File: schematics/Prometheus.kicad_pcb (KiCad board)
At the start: 2 copper layers, 170.2 x 170.2 mm, 57 parts, among them J1 ATX Power Conn, J10 Centronics, J11 ps/2 keyb, J12 Expansion, J13 Joy1, J14 Joy2, J15 rs232, J16 DIN41612_02x32_AB, J17 DIN41612_02x32_AB, J2 FDC Connector, J3 IDE Connector, J4 JTAG, J5 Left Audio, J6 Right Audio, J7 GRACE board interface 1, J8 GRACE board interface 2, J9 15kHz Video Out, SW1 Power Switch, SW2 Reset Switch, U1 DS1501YN, U10 2764, U11 EN5503DOC, U12 VRAM, U13 wdc65c22, U14 wdc65c51, U15 MAX233CPP, U16 wdc65c22, U17 41464, U18 41464, U19 41464, U2 wdc65c816, U20 41464, U3 WD1772, U8 XC9572XL-TQ100, X1 32kHz, X2 8MHz, X3 1.8432MHz

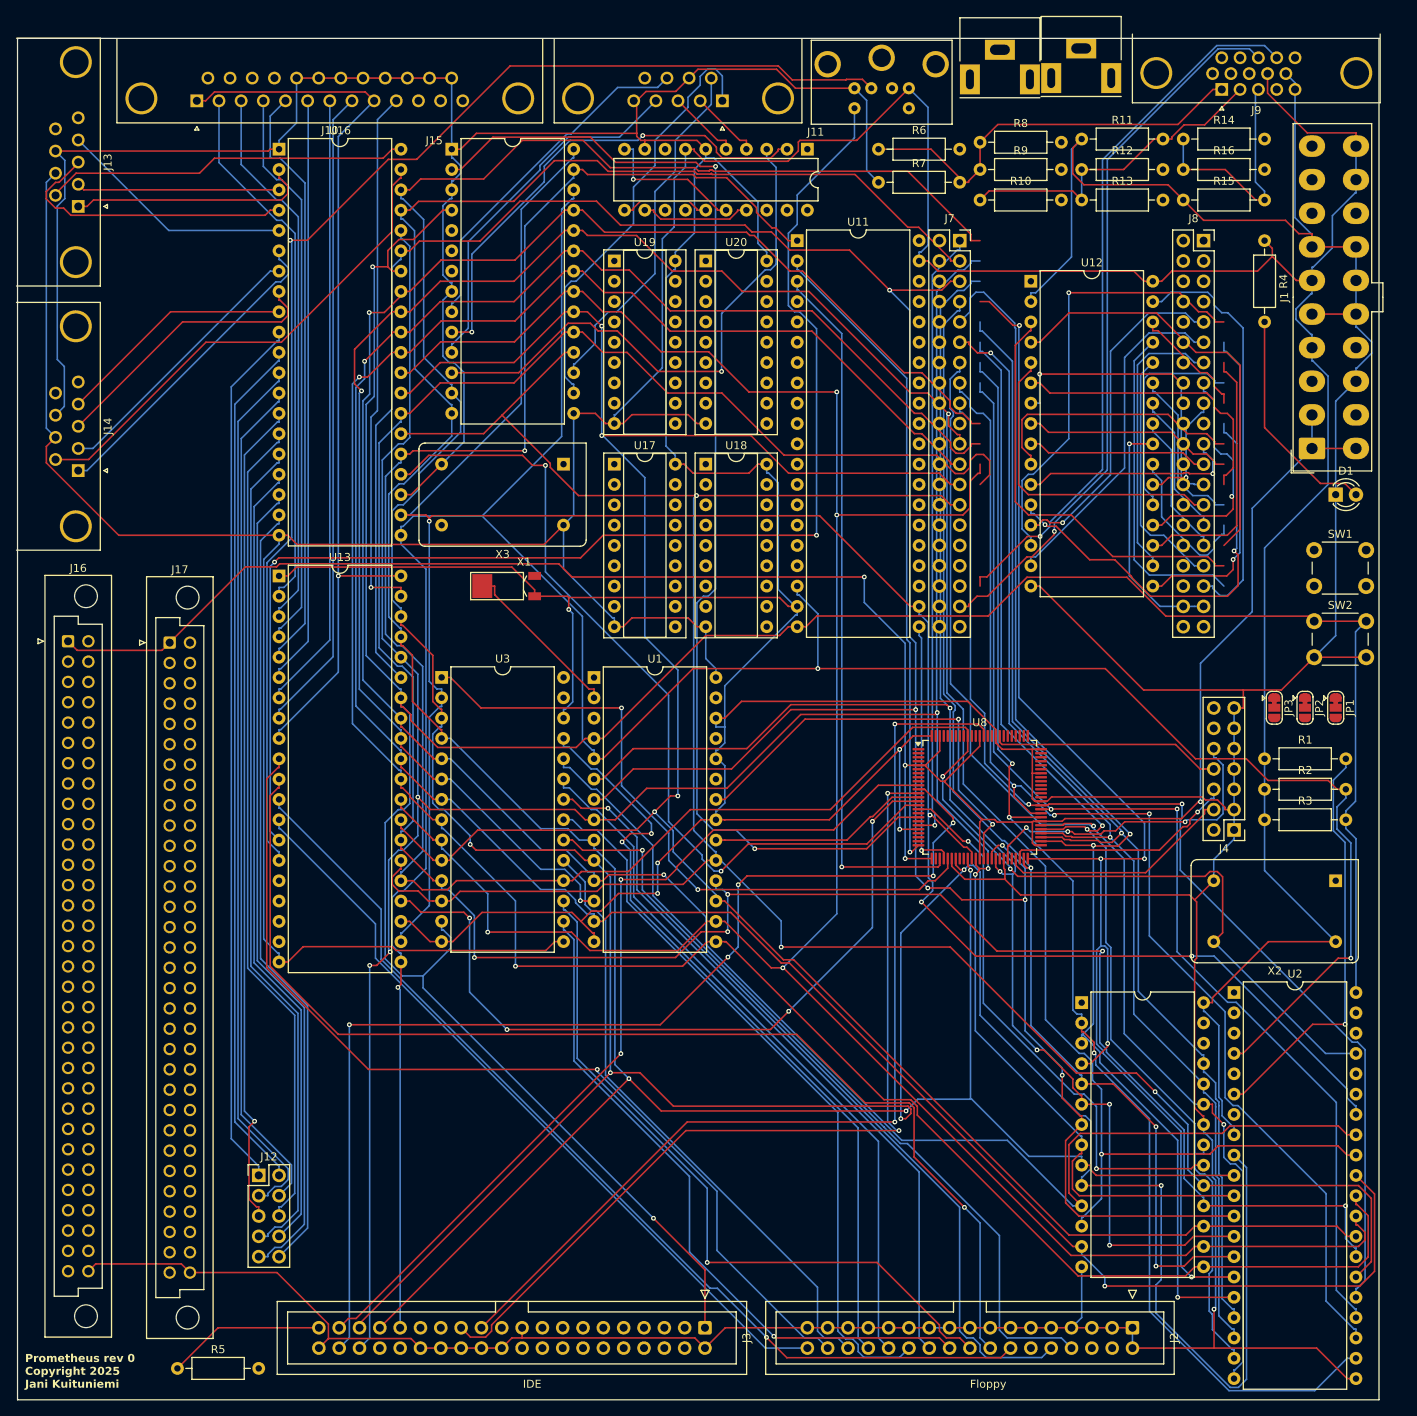
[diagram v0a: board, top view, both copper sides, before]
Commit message: Initial PCB layout and route.
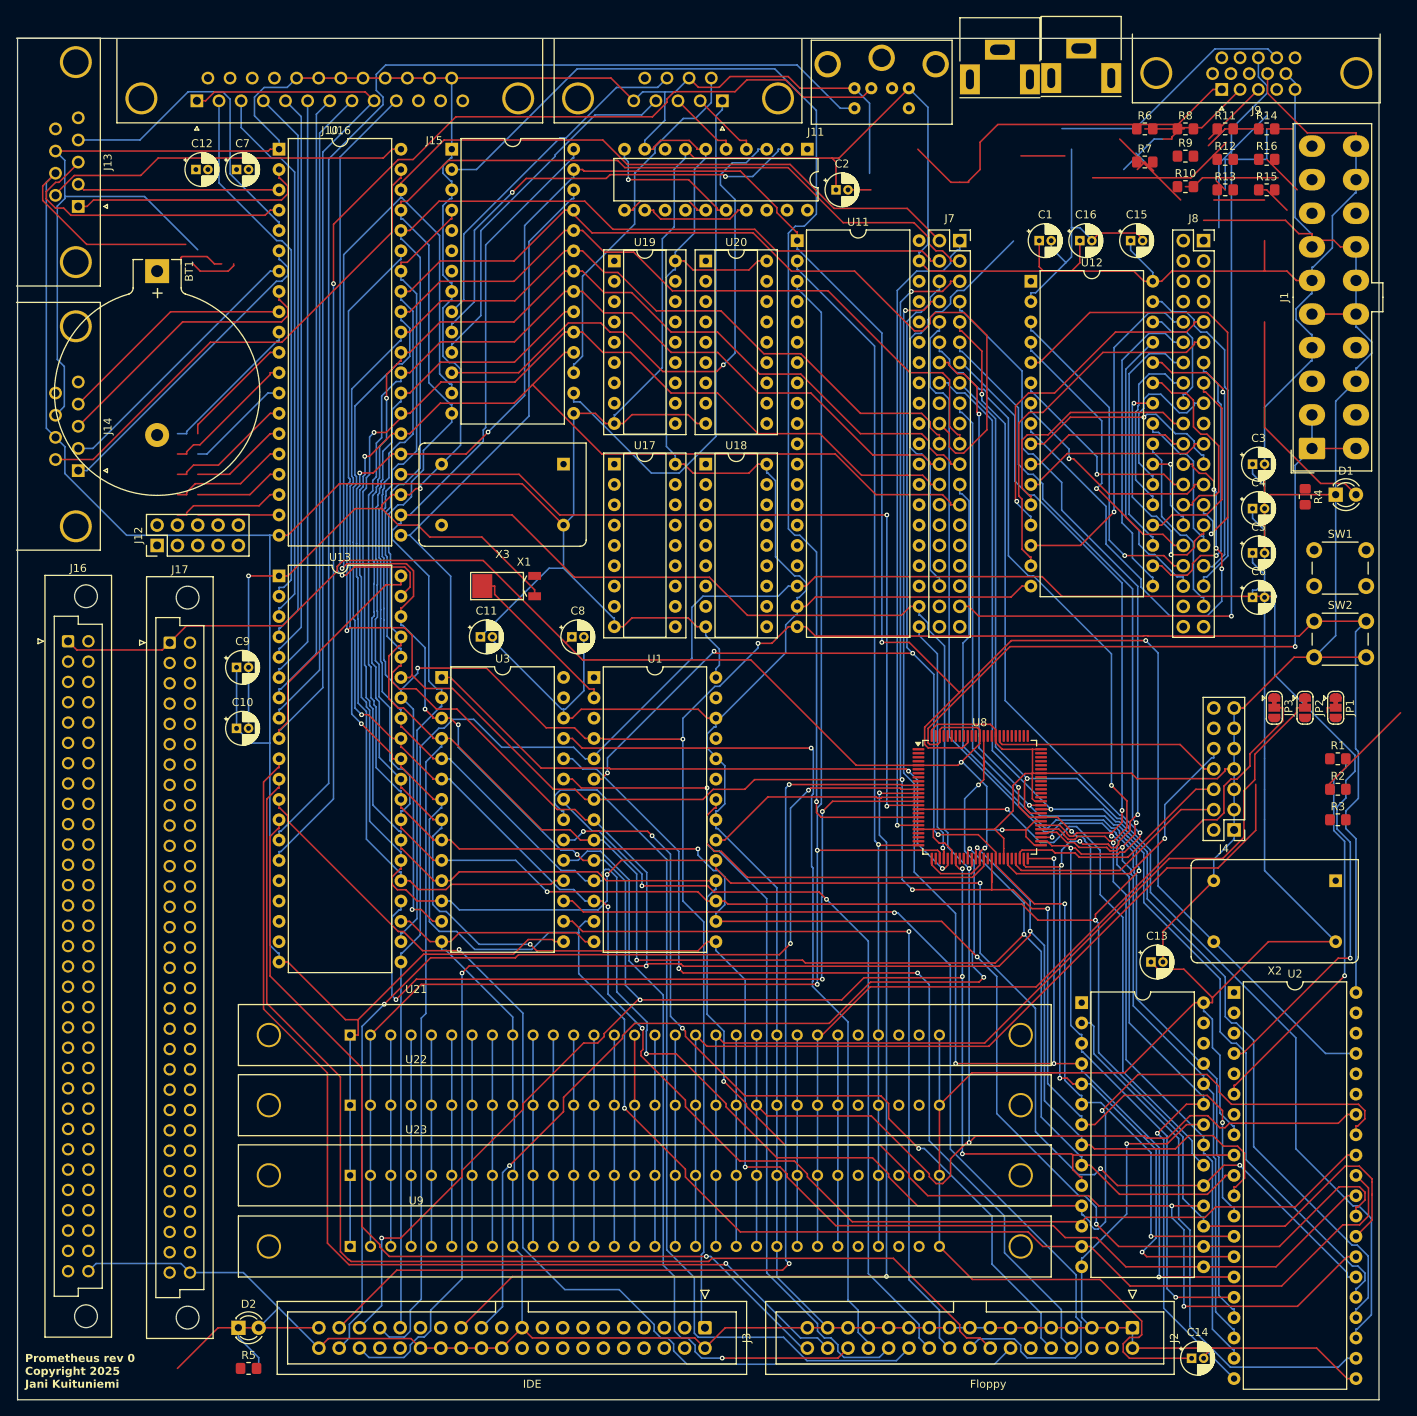
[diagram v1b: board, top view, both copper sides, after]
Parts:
- added BT1: Battery, Battery:BatteryHolder_Keystone_104_1x23mm, F.Cu at (125.7, 47.0)
- added C1: 0.1uF, Capacitor_THT:CP_Radial_D4.0mm_P1.50mm, F.Cu at (236.0, 43.2)
- added C10: 0.1uF, Capacitor_THT:CP_Radial_D4.0mm_P1.50mm, F.Cu at (135.7, 104.1)
- added C11: 0.1uF, Capacitor_THT:CP_Radial_D4.0mm_P1.50mm, F.Cu at (166.1, 92.7)
- added C12: C, Capacitor_THT:CP_Radial_D4.0mm_P1.50mm, F.Cu at (130.6, 34.3)
- added C13: C, Capacitor_THT:CP_Radial_D4.0mm_P1.50mm, F.Cu at (250.0, 133.3)
- added C14: C, Capacitor_THT:CP_Radial_D4.0mm_P1.50mm, F.Cu at (255.0, 182.9)
- added C15: C, Capacitor_THT:CP_Radial_D4.0mm_P1.50mm, F.Cu at (247.4, 43.2)
- added C16: C, Capacitor_THT:CP_Radial_D4.0mm_P1.50mm, F.Cu at (241.1, 43.2)
- added C2: 0.1uF, Capacitor_THT:CP_Radial_D4.0mm_P1.50mm, F.Cu at (210.6, 36.8)
- added C3: 0.1uF, Capacitor_THT:CP_Radial_D4.0mm_P1.50mm, F.Cu at (262.7, 71.1)
- added C4: 0.1uF, Capacitor_THT:CP_Radial_D4.0mm_P1.50mm, F.Cu at (262.7, 76.7)
- added C5: 0.1uF, Capacitor_THT:CP_Radial_D4.0mm_P1.50mm, F.Cu at (262.7, 82.2)
- added C6: 0.1uF, Capacitor_THT:CP_Radial_D4.0mm_P1.50mm, F.Cu at (262.7, 87.8)
- added C7: 0.1uF, Capacitor_THT:CP_Radial_D4.0mm_P1.50mm, F.Cu at (135.7, 34.3)
- added C8: 0.1uF, Capacitor_THT:CP_Radial_D4.0mm_P1.50mm, F.Cu at (177.6, 92.7)
- added C9: 0.1uF, Capacitor_THT:CP_Radial_D4.0mm_P1.50mm, F.Cu at (135.7, 96.5)
- added D2: IDE LED, LED_THT:LED_D3.0mm, F.Cu at (135.9, 179.1)
- added U21: SIMM16M, Custom_Socket:SIMM, F.Cu at (186.7, 142.5)
- added U22: SIMM16M, Custom_Socket:SIMM, F.Cu at (186.7, 151.2)
- added U23: SIMM16M, Custom_Socket:SIMM, F.Cu at (186.7, 160.0)
- added U9: SIMM16M, Custom_Socket:SIMM, F.Cu at (186.7, 168.9)
- R1, R10, R11, R12, R13, R14, R15, R16, R2, R3, R4, R5, R6, R7, R8, R9: footprint Resistor_THT:R_Axial_DIN0207_L6.3mm_D2.5mm_P10.16mm_Horizontal -> Resistor_SMD:R_0805_2012Metric_Pad1.20x1.40mm_HandSolder
- moved J12 79.8 mm to (125.7, 81.3), turned to 90 degrees
- moved R6 33.4 mm to (249.2, 29.2)
- moved R7 33.4 mm to (249.2, 33.4)
- moved R4 32.4 mm to (269.2, 75.2)
- moved R10 25.7 mm to (254.3, 36.4)
- moved R8 25.7 mm to (254.3, 29.2)
- moved R9 25.7 mm to (254.3, 32.6)
- moved R11 18.0 mm to (259.2, 29.2)
- moved R12 18.0 mm to (259.2, 33.0)
- moved R13 18.0 mm to (259.2, 36.8)
- moved R14 10.5 mm to (264.4, 29.2)
- moved R15 10.5 mm to (264.4, 36.8)
- moved R16 10.5 mm to (264.4, 33.0)
- moved R1 9.16 mm to (273.3, 108.0)
- moved R2 9.16 mm to (273.3, 111.8)
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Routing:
- net Vcc: track 583.2 -> 822.7 mm
- net MA9: track 1.30 -> 129.6 mm
- net MA10: track 1.30 -> 124.8 mm
- net MA11: track 1.30 -> 107.7 mm
- net CAS: track 88.8 -> 190.8 mm, vias 1 -> 2
- net Net-(J12-Pin_3): track 110.4 -> 17.2 mm
- net Net-(J12-Pin_2): track 107.5 -> 15.0 mm
- net Net-(J12-Pin_4): track 105.6 -> 13.3 mm
- net Net-(J12-Pin_6): track 103.0 -> 12.3 mm
- net Net-(J12-Pin_1): track 109.4 -> 18.8 mm
- net Net-(J12-Pin_7): track 105.0 -> 15.0 mm
- net Net-(J12-Pin_8): track 100.2 -> 11.2 mm
- net Net-(J12-Pin_9): track 102.5 -> 13.9 mm
- net Net-(J12-Pin_5): track 103.7 -> 16.0 mm, vias 1 -> 0
- net Net-(J12-Pin_10): track 97.7 -> 10.2 mm
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
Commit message: Added a lot of missing footprints in the audio-section. Adjusted the PCB layout and re-routed the board.
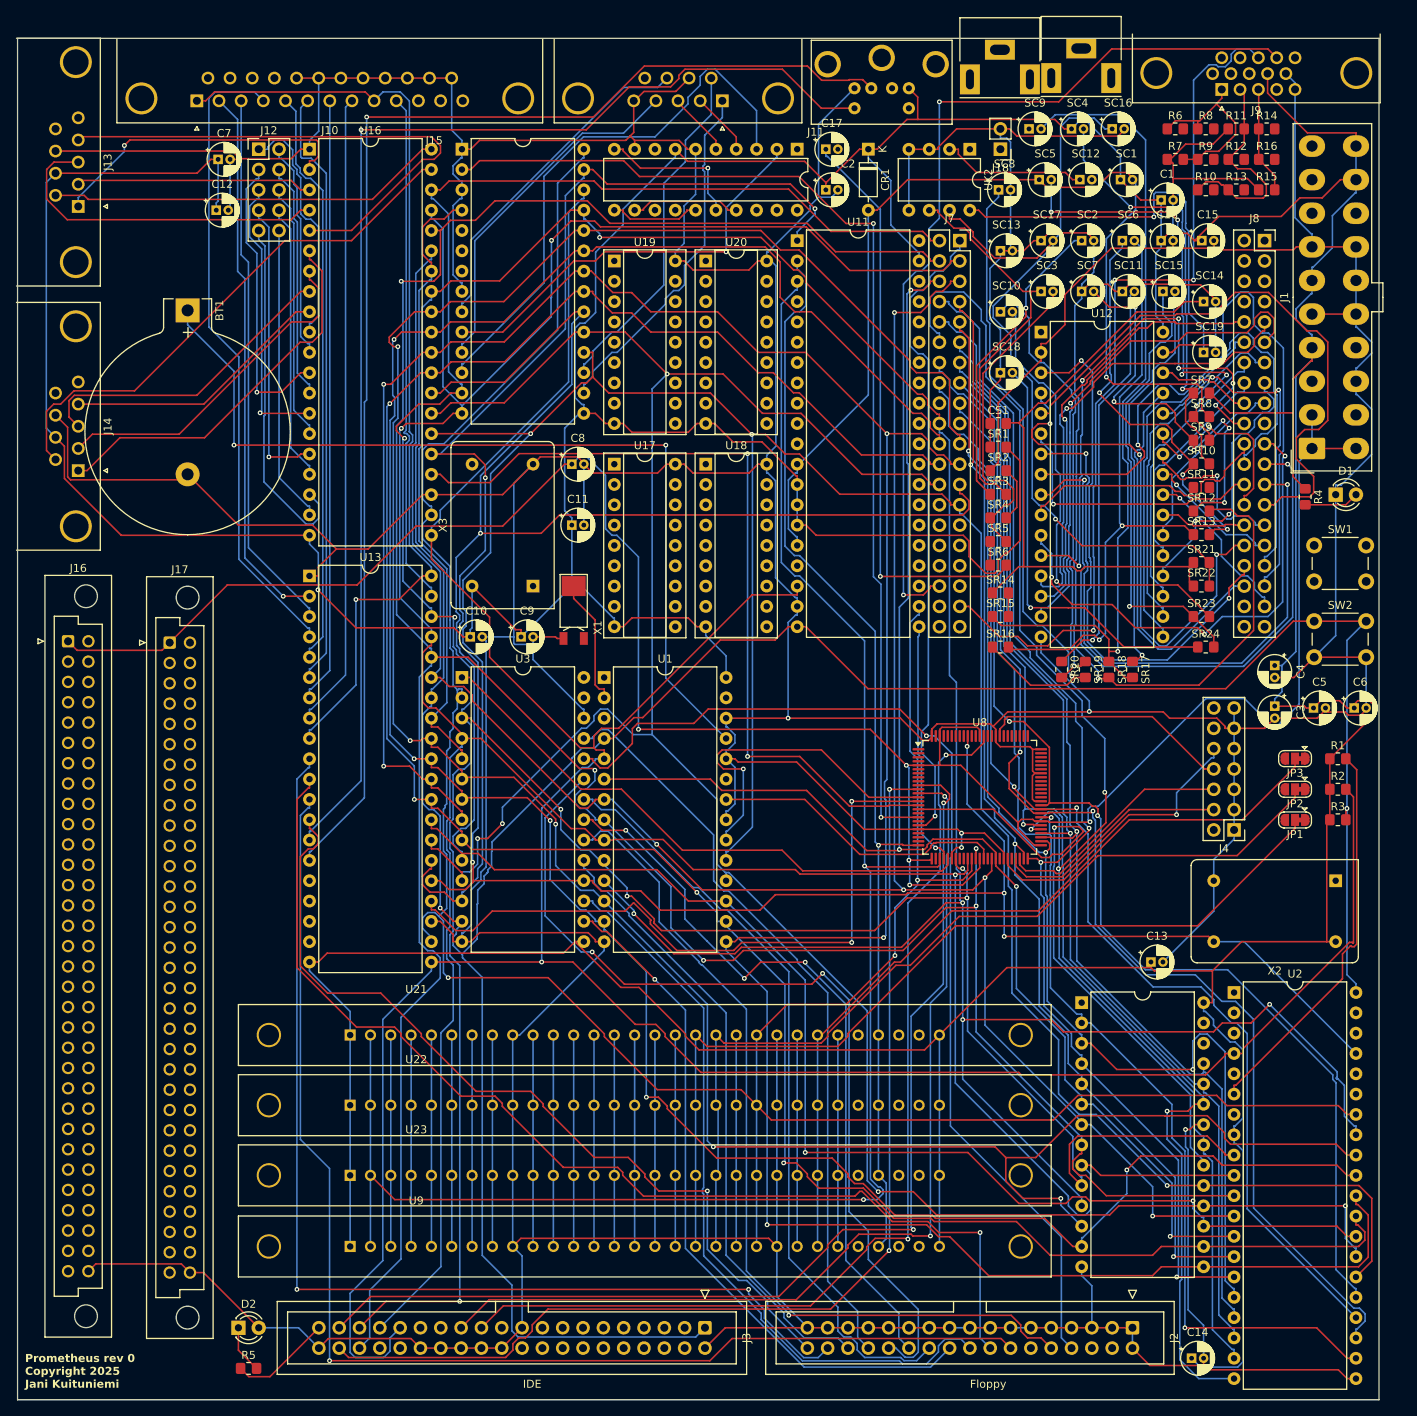
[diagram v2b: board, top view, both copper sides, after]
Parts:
- added C17: 0.1u, Capacitor_THT:CP_Radial_D4.0mm_P1.50mm, F.Cu at (209.3, 31.8)
- added CR1: 1N914, Diode_THT:D_DO-35_SOD27_P7.62mm_Horizontal, F.Cu at (214.6, 31.8)
- added CS1: .1u, Resistor_SMD:R_0805_2012Metric_Pad1.20x1.40mm_HandSolder, F.Cu at (230.9, 66.0)
- added J18: SPEAKER, Connector_PinHeader_2.54mm:PinHeader_1x02_P2.54mm_Vertical, F.Cu at (231.1, 31.8)
- added SC1: 10p, Capacitor_THT:CP_Radial_D4.0mm_P1.50mm, F.Cu at (246.2, 35.6)
- added SC10: 3.9n, Capacitor_THT:CP_Radial_D4.0mm_P1.50mm, F.Cu at (231.1, 52.1)
- added SC11: 220p, Capacitor_THT:CP_Radial_D4.0mm_P1.50mm, F.Cu at (246.4, 49.5)
- added SC12: .1u, Capacitor_THT:CP_Radial_D4.0mm_P1.50mm, F.Cu at (241.1, 35.6)
- added SC13: 1.8n, Capacitor_THT:CP_Radial_D4.0mm_P1.50mm, F.Cu at (231.1, 44.5)
- added SC14: 470u/16v, Capacitor_THT:CP_Radial_D4.0mm_P1.50mm, F.Cu at (256.5, 50.8)
- added SC15: 3.9n, Capacitor_THT:CP_Radial_D4.0mm_P1.50mm, F.Cu at (251.5, 49.5)
- added SC16: 22u, Capacitor_THT:CP_Radial_D4.0mm_P1.50mm, F.Cu at (245.1, 29.2)
- added SC17: .1u, Capacitor_THT:CP_Radial_D4.0mm_P1.50mm, F.Cu at (236.2, 43.2)
- added SC18: 560p, Capacitor_THT:CP_Radial_D4.0mm_P1.50mm, F.Cu at (231.1, 59.7)
- added SC19: 22u, Capacitor_THT:CP_Radial_D4.0mm_P1.50mm, F.Cu at (256.5, 57.1)
- added SC2: .1u, Capacitor_THT:CP_Radial_D4.0mm_P1.50mm, F.Cu at (241.3, 43.2)
- added SC3: 22u, Capacitor_THT:CP_Radial_D4.0mm_P1.50mm, F.Cu at (236.2, 49.5)
- added SC4: 10p, Capacitor_THT:CP_Radial_D4.0mm_P1.50mm, F.Cu at (240.0, 29.2)
- added SC5: 10p, Capacitor_THT:CP_Radial_D4.0mm_P1.50mm, F.Cu at (236.0, 35.6)
- added SC6: 10p, Capacitor_THT:CP_Radial_D4.0mm_P1.50mm, F.Cu at (246.4, 43.2)
- added SC7: 10p, Capacitor_THT:CP_Radial_D4.0mm_P1.50mm, F.Cu at (241.3, 49.5)
- added SC8: 1.5n, Capacitor_THT:CP_Radial_D4.0mm_P1.50mm, F.Cu at (230.9, 36.8)
- added SC9: 22u, Capacitor_THT:CP_Radial_D4.0mm_P1.50mm, F.Cu at (234.7, 29.2)
- added SR1: 1K, Resistor_SMD:R_0805_2012Metric_Pad1.20x1.40mm_HandSolder, F.Cu at (230.9, 69.0)
- added SR10: 3.9K, Resistor_SMD:R_0805_2012Metric_Pad1.20x1.40mm_HandSolder, F.Cu at (256.3, 71.1)
- added SR11: 200K, Resistor_SMD:R_0805_2012Metric_Pad1.20x1.40mm_HandSolder, F.Cu at (256.3, 74.0)
- added SR12: 3.9K, Resistor_SMD:R_0805_2012Metric_Pad1.20x1.40mm_HandSolder, F.Cu at (256.3, 77.0)
- added SR13: 3.9K, Resistor_SMD:R_0805_2012Metric_Pad1.20x1.40mm_HandSolder, F.Cu at (256.3, 79.9)
- added SR14: 470K, Resistor_SMD:R_0805_2012Metric_Pad1.20x1.40mm_HandSolder, F.Cu at (231.1, 87.2)
- added SR15: 470K, Resistor_SMD:R_0805_2012Metric_Pad1.20x1.40mm_HandSolder, F.Cu at (231.1, 90.2)
- added SR16: 15K, Resistor_SMD:R_0805_2012Metric_Pad1.20x1.40mm_HandSolder, F.Cu at (231.1, 94.0)
- added SR17: 10K, Resistor_SMD:R_0805_2012Metric_Pad1.20x1.40mm_HandSolder, F.Cu at (247.7, 96.8)
- added SR18: 10K, Resistor_SMD:R_0805_2012Metric_Pad1.20x1.40mm_HandSolder, F.Cu at (244.7, 96.8)
- added SR19: 15K, Resistor_SMD:R_0805_2012Metric_Pad1.20x1.40mm_HandSolder, F.Cu at (241.8, 96.8)
- added SR2: 560, Resistor_SMD:R_0805_2012Metric_Pad1.20x1.40mm_HandSolder, F.Cu at (230.9, 71.9)
- added SR20: 15K, Resistor_SMD:R_0805_2012Metric_Pad1.20x1.40mm_HandSolder, F.Cu at (238.8, 96.8)
- added SR21: 200, Resistor_SMD:R_0805_2012Metric_Pad1.20x1.40mm_HandSolder, F.Cu at (256.3, 83.4)
- added SR22: 200, Resistor_SMD:R_0805_2012Metric_Pad1.20x1.40mm_HandSolder, F.Cu at (256.3, 86.4)
- added SR23: 10K, Resistor_SMD:R_0805_2012Metric_Pad1.20x1.40mm_HandSolder, F.Cu at (256.3, 90.2)
- added SR24: 10K, Resistor_SMD:R_0805_2012Metric_Pad1.20x1.40mm_HandSolder, F.Cu at (256.8, 94.0)
- added SR3: 2.7, Resistor_SMD:R_0805_2012Metric_Pad1.20x1.40mm_HandSolder, F.Cu at (230.9, 74.9)
- added SR4: 1K, Resistor_SMD:R_0805_2012Metric_Pad1.20x1.40mm_HandSolder, F.Cu at (230.9, 77.8)
- added SR5: 220, Resistor_SMD:R_0805_2012Metric_Pad1.20x1.40mm_HandSolder, F.Cu at (230.9, 80.8)
- added SR6: 100, Resistor_SMD:R_0805_2012Metric_Pad1.20x1.40mm_HandSolder, F.Cu at (230.9, 83.7)
- added SR7: 3.9K, Resistor_SMD:R_0805_2012Metric_Pad1.20x1.40mm_HandSolder, F.Cu at (256.3, 62.2)
- added SR8: 3.9K, Resistor_SMD:R_0805_2012Metric_Pad1.20x1.40mm_HandSolder, F.Cu at (256.3, 65.2)
- added SR9: 3.9K, Resistor_SMD:R_0805_2012Metric_Pad1.20x1.40mm_HandSolder, F.Cu at (256.3, 68.1)
- added UK2: LM380N-8, Package_DIP:DIP-8_W7.62mm, F.Cu at (227.3, 31.8)
- moved J12 51.1 mm to (138.4, 31.8), turned to 0 degrees
- moved C9 35.8 mm to (171.2, 92.7)
- moved C10 31.4 mm to (164.9, 92.7)
- moved C3 30.4 mm to (265.4, 101.4), turned to -90 degrees
- moved C8 21.6 mm to (177.6, 71.1)
- moved C5 20.8 mm to (270.3, 101.6)
- moved C4 19.8 mm to (265.4, 96.3), turned to -90 degrees
- moved C6 18.8 mm to (275.4, 101.6)
- moved C11 18.1 mm to (177.6, 78.7)
- moved C1 16.1 mm to (251.2, 38.1)
- moved X3 15.7 mm to (172.7, 86.4), turned to 90 degrees
- moved JP1 14.9 mm to (268.0, 115.6), turned to 180 degrees
- moved JP2 10.3 mm to (268.0, 111.8), turned to 180 degrees
- moved C16 10.2 mm to (251.2, 43.2)
- moved X1 8.92 mm to (177.8, 89.4), turned to 180 degrees
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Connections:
- J1 pad 18: unconnected-(J1-Pin_18-Pad18) -> -5V 
- U11 pad 11: unconnected-(U11-VVREF-Pad11) -> /Audio/-5V
- U11 pad 12: unconnected-(U11-VOLFDBK-Pad12) -> /Audio/SND-SIG-
- U11 pad 13: unconnected-(U11-VOL--Pad13) -> Vcc
- U11 pad 14: unconnected-(U11-WVREF-Pad14) -> Vcc
- U11 pad 15: Net-(U11-SIG+) -> Vcc
- U11 pad 16: Net-(U11-SIG-) -> /Audio/SND-SIG-
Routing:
- net GNDA: track 0.00 -> 217.5 mm, vias 0 -> 1
- net /Audio/SND-SIG-: track 0.00 -> 126.0 mm, vias 0 -> 1
- net Net-(BT1-+): track 0.00 -> 113.0 mm, vias 0 -> 2
- net +12V: track 0.00 -> 105.4 mm, vias 0 -> 1
- net Net-(SC9-Pad2): track 0.00 -> 104.4 mm, vias 0 -> 1
- net Vcc: track 822.7 -> 908.0 mm, vias 0 -> 1
- net Net-(SC8-Pad1): track 0.00 -> 80.5 mm, vias 0 -> 1
- net Net-(SD1-K): track 0.00 -> 79.0 mm
- net Net-(SC6-Pad2): track 0.00 -> 74.6 mm, vias 0 -> 2
- net GNDPWR: track 0.00 -> 72.8 mm, vias 0 -> 1
- net Net-(UL2B--): track 0.00 -> 57.6 mm, vias 0 -> 1
- net Net-(SC5-Pad2): track 0.00 -> 56.5 mm, vias 0 -> 5
- net Net-(SC15-Pad1): track 0.00 -> 56.3 mm, vias 0 -> 1
- net Net-(SC10-Pad1): track 0.00 -> 55.4 mm, vias 0 -> 1
- net Net-(SC4-Pad2): track 0.00 -> 53.8 mm, vias 0 -> 3
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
